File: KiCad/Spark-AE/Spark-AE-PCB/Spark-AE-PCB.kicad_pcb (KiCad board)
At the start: 2 copper layers, 50 x 100 mm, 21 parts, among them J1 SSM-120-L-SV-BE, J2 SSM-120-L-SV-BE, J3 Conn_02x10_Odd_Even, J4 Conn_02x05_Odd_Even, J5 Conn_01x08_Socket, J6 Conn_01x08_Socket, J7 UJ32-C-V-G-TH-5-P24-TR, SW1 SW_Push, SW2 SW_Push, U1 PJS008U-3000-0, U2 Daisy_Seed

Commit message: moving over progress from "Shock" (see desc)
I attempted to create this Daisy Pod clone as an AE-1U module called the "Shock". As expected I couldn't make it work.

I've moved my progress on the "Shock" schematic over to and replacing the work on the "Spark".

I plan to go back to make the "Shock" a stripped down version of the "Spark" in an AE-1U format.
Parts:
- removed ? (x5): , 
- removed J1, J2: SSM-120-L-SV-BE, clectric-diy:SAMTEC_SSM-120-L-SV-BE
- removed J3: Conn_02x10_Odd_Even, Connector_PinHeader_2.54mm:PinHeader_2x10_P2.54mm_Vertical
- removed J4: Conn_02x05_Odd_Even, Connector_PinHeader_2.54mm:PinHeader_2x05_P2.54mm_Vertical
- removed J5, J6: Conn_01x08_Socket, Connector_PinSocket_2.54mm:PinSocket_1x08_P2.54mm_Vertical
- removed J7: UJ32-C-V-G-TH-5-P24-TR, clectric-diy:SAMESKY_UJ32-C-V-G-TH-5-P24-TR
- removed LED1, LED2: WS2812B-V5/W, clectric-diy:LED-SMD_4P-L5.0-W5.0-TL-1
- removed R1, R2: RK09K1130A8G, clectric-diy:RES-TH_RK09K113004U
- removed S1: PEL12T-4225S-S1024, clectric-diy:PEL12T4225SS1024
- removed SW1, SW2: SW_Push, Button_Switch_THT:SW_PUSH_6mm
- removed U1: PJS008U-3000-0, clectric-diy:PJS008U-3000-0
- removed U2: Daisy_Seed, clectric-diy:DAISY_SEED
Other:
- board outline removed

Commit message: initial committ of completely reworked schematic. thanks gemini!
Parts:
- added ENC1: PEL12T-4225S-S1024, clectric-diy:PEL12T4225SS1024, F.Cu at (119.6, 129.2)
- added J1: Conn_01x20_Pin, clectric-diy:Connector_PinSocket-1x20-P2.54mm_Mill-Max_315-13-120-41-004000, B.Cu at (134.3, 122.5)
- added J2: Conn_01x20_Pin, clectric-diy:Connector_PinSocket-1x20-P2.54mm_Mill-Max_315-13-120-41-004000, B.Cu at (149.6, 74.2)
- added J3: Conn_01x09_Socket, Connector_PinSocket_2.54mm:PinSocket_1x09_P2.54mm_Vertical, F.Cu at (109.3, 49.8)
- added J4: Conn_01x09_Socket, Connector_PinSocket_2.54mm:PinSocket_1x09_P2.54mm_Vertical, F.Cu at (154.7, 49.8)
- added J5: Conn_02x05_Odd_Even, Connector_PinHeader_2.54mm:PinHeader_2x05_P2.54mm_Vertical, B.Cu at (154.7, 128.8)
- added LED1: A-SP1943B1GHR6C-C01-2T, clectric-diy:LED-SMD_4P-L1.6-W1.5-BL_A-SP1943B1GHR6C-C01-2T, F.Cu at (119.6, 97.7)
- added LED2: A-SP1943B1GHR6C-C01-2T, clectric-diy:LED-SMD_4P-L1.6-W1.5-BL_A-SP1943B1GHR6C-C01-2T, F.Cu at (119.6, 112.9)
- added POT1: RK09K1130D62, clectric-diy:RK09K1130D62, F.Cu at (119.6, 101.2)
- added POT2: RK09K1130D62, clectric-diy:RK09K1130D62, F.Cu at (119.6, 116.4)
- added SW1: SW_Push, Button_Switch_THT:SW_PUSH_6mm, F.Cu at (145.2, 79.1)
- added SW2: SW_Push, Button_Switch_THT:SW_PUSH_6mm, F.Cu at (145.2, 91.1)
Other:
- board outline added: 50 x 100 mm
- board text added: "&"

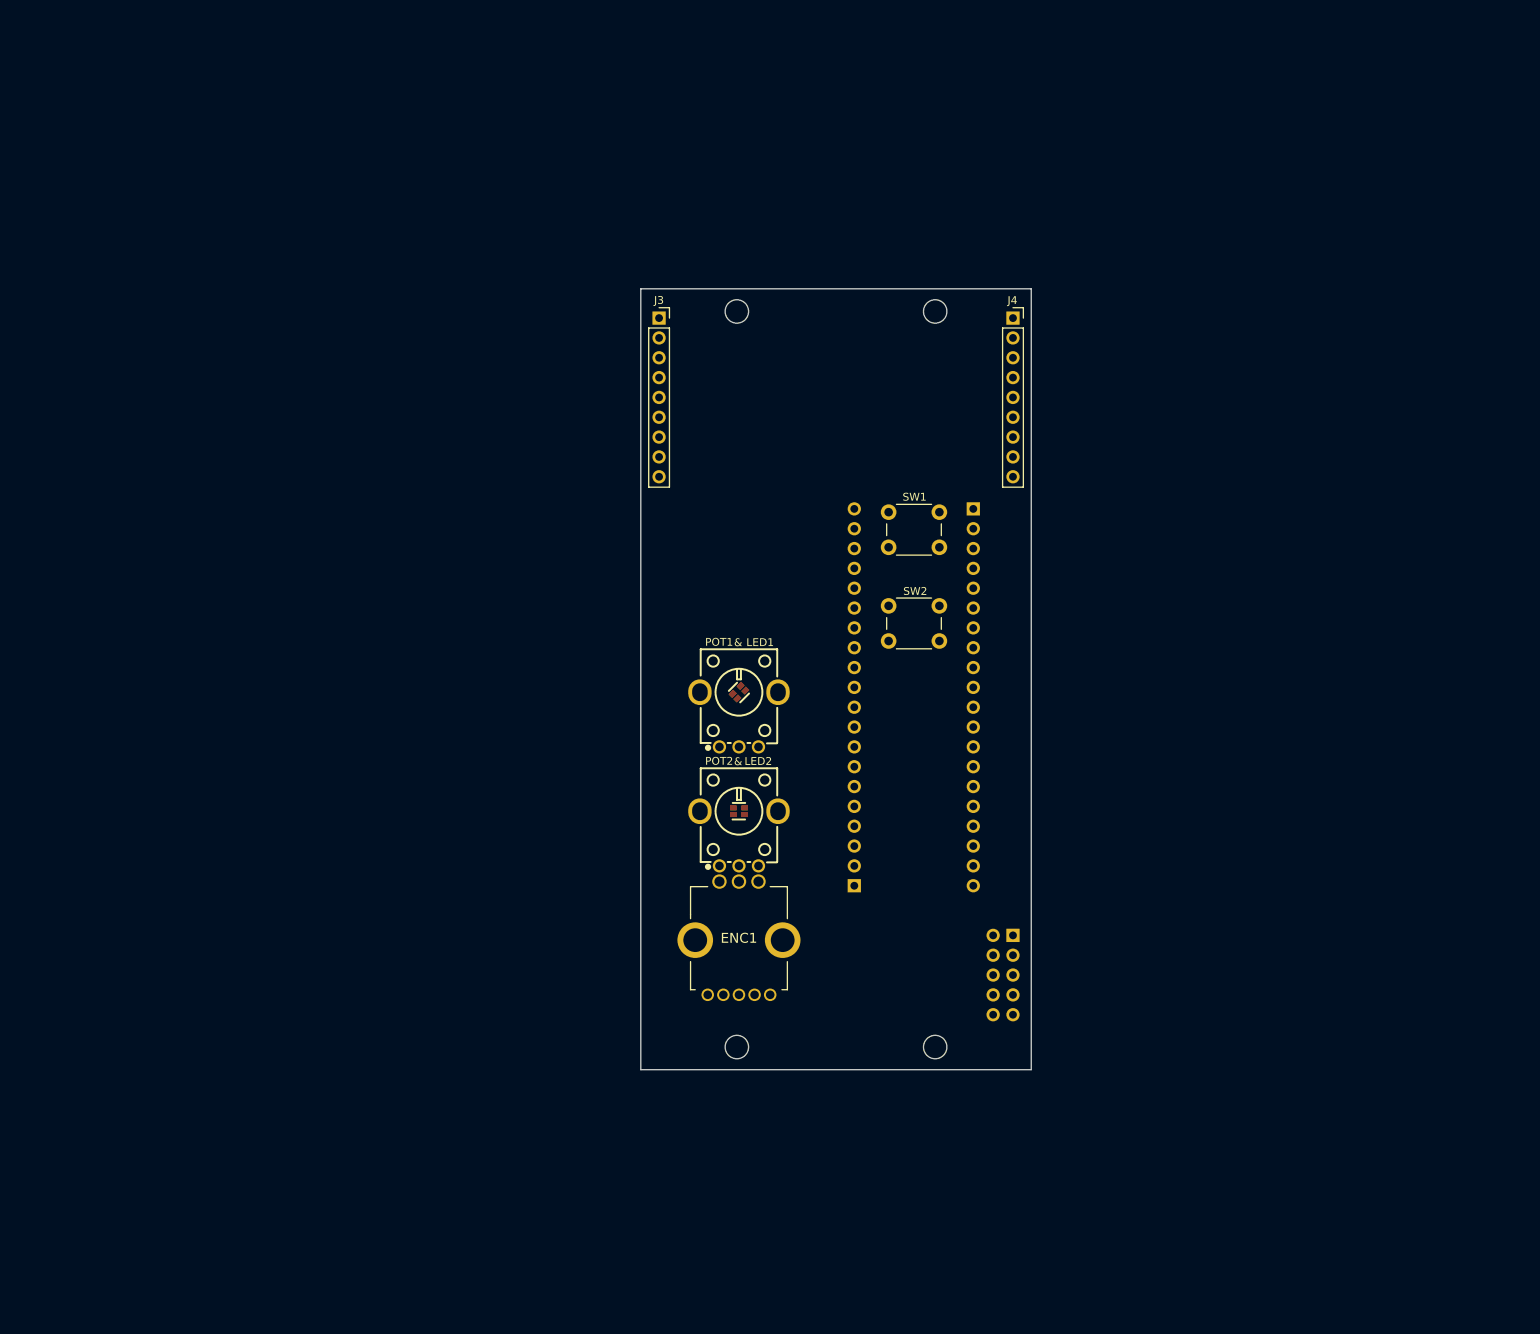
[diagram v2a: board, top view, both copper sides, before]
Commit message: assigned footprints & sorted ratsnest
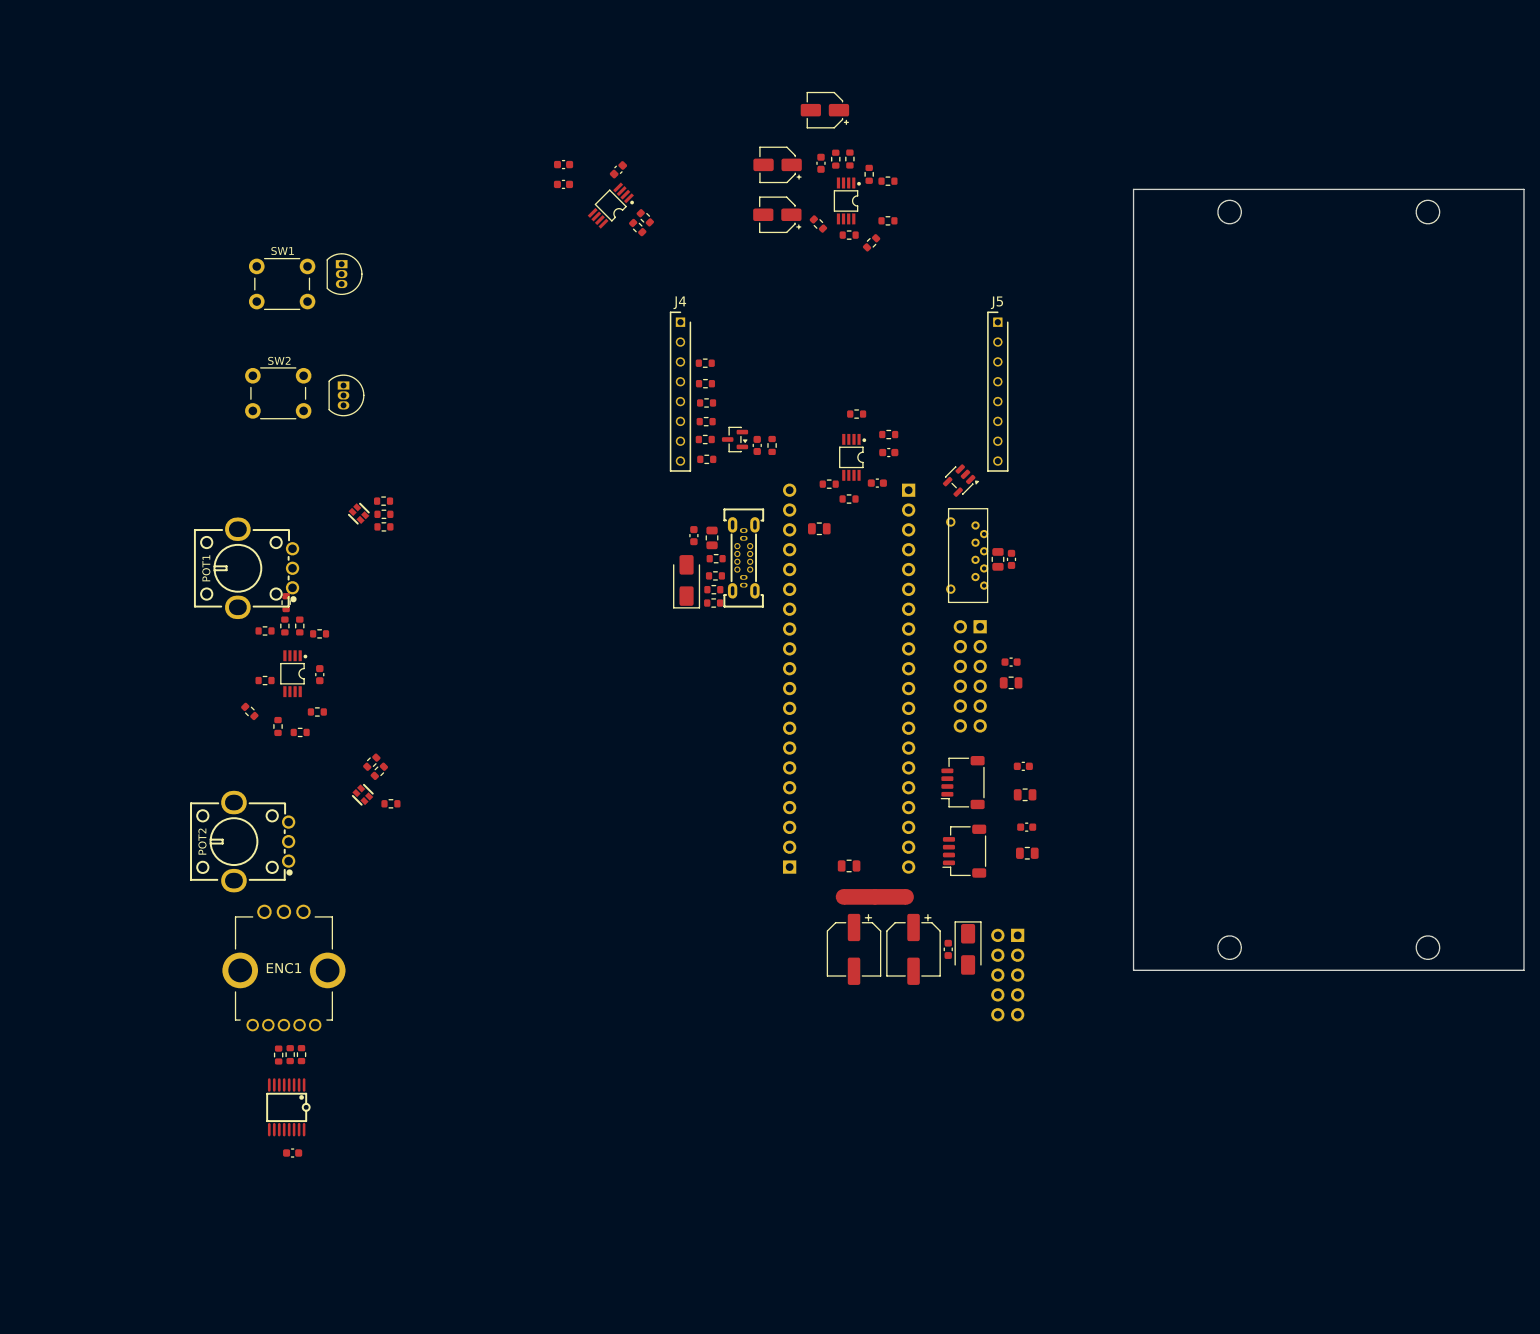
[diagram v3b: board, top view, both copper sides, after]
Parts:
- added C1: 220uF, Capacitor_SMD:CP_Elec_6.3x5.4, F.Cu at (134.3, 130.6)
- added C10: 10uF, Capacitor_SMD:CP_Elec_4x5.4, F.Cu at (124.5, 30.1)
- added C11: 10uF, Capacitor_SMD:CP_Elec_4x5.4, F.Cu at (124.5, 36.5)
- added C12: 100nF, Capacitor_SMD:C_0603_1608Metric, F.Cu at (130.1, 29.9)
- added C13: 10uF, Capacitor_SMD:CP_Elec_4x5.4, F.Cu at (130.6, 23.1)
- added C14: 10uF, Capacitor_SMD:C_0805_2012Metric, F.Cu at (152.7, 80.7)
- added C15: 100nF, Capacitor_SMD:C_0603_1608Metric, F.Cu at (154.5, 80.7)
- added C16: 10nF, Capacitor_SMD:C_0603_1608Metric, F.Cu at (121.9, 66.1)
- added C17: 100nF, Capacitor_SMD:C_0603_1608Metric, F.Cu at (137.3, 70.9)
- added C18: 100nF, Capacitor_SMD:C_0603_1608Metric, F.Cu at (138.7, 67.0)
- added C19: 100nF, Capacitor_SMD:C_0603_1608Metric, F.Cu at (113.8, 77.6)
- added C2: 220uF, Capacitor_SMD:CP_Elec_6.3x5.4, F.Cu at (141.9, 130.6)
- added C20: 10uF, Capacitor_SMD:C_0805_2012Metric, F.Cu at (116.1, 77.9)
- added C21: 100nF, Capacitor_SMD:C_0603_1608Metric, F.Cu at (156.0, 107.2)
- added C22: 10uF, Capacitor_SMD:C_0805_2012Metric, F.Cu at (156.2, 110.8)
- added C23: 100nF, Capacitor_SMD:C_0603_1608Metric, F.Cu at (156.4, 115.0)
- added C24: 10uF, Capacitor_SMD:C_0805_2012Metric, F.Cu at (156.5, 118.3)
- added C25: 100nF, Capacitor_SMD:C_0603_1608Metric, F.Cu at (154.4, 93.8)
- added C26: 10uF, Capacitor_SMD:C_0805_2012Metric, F.Cu at (154.4, 96.5)
- added C3: 10uF, Capacitor_SMD:C_0805_2012Metric, F.Cu at (129.8, 76.7)
- added C4: 10uF, Capacitor_SMD:C_0805_2012Metric, F.Cu at (133.7, 119.9)
- added C5: 100nF, Capacitor_SMD:C_0603_1608Metric, F.Cu at (65.9, 95.4)
- added C6: 100nF, Capacitor_SMD:C_0603_1608Metric, F.Cu at (62.4, 156.7)
- added C7: 1uF, Capacitor_SMD:C_0603_1608Metric, F.Cu at (97.1, 30.1)
- added C8: 1uF, Capacitor_SMD:C_0603_1608Metric, F.Cu at (97.1, 32.6)
- added C9: 100nF, Capacitor_SMD:C_0603_1608Metric, F.Cu at (104.1, 30.8)
- added D1: SS14, Diode_SMD:D_SMA, F.Cu at (148.9, 130.6)
- added D2: BAT54S, Package_TO_SOT_SMD:SOT-23, F.Cu at (119.1, 65.3)
- added D3: 2214, Diode_SMD:D_SMA, F.Cu at (112.8, 83.4)
- added FB1: BLM18AG601, Inductor_SMD:L_0603_1608Metric, F.Cu at (146.4, 130.6)
- added J6: I2C_IN, Connector_JST:JST_SH_SM04B-SRSS-TB_1x04-1MP_P1.00mm_Horizontal, F.Cu at (148.3, 109.2)
- added J7: I2C_OUT, Connector_JST:JST_SH_SM04B-SRSS-TB_1x04-1MP_P1.00mm_Horizontal, F.Cu at (148.5, 118.0)
- added J8: Conn_02x06_Top_Bottom, Connector_PinHeader_2.54mm:PinHeader_2x06_P2.54mm_Vertical, B.Cu at (150.4, 89.3)
- added NT1: NetTie_3_Tee, NetTie:NetTie-3_SMD_Pad2.0mm, F.Cu at (137.0, 123.9)
- added Q1: 2N3904, Package_TO_SOT_THT:TO-92_Inline, F.Cu at (68.7, 42.9)
- added Q2: 2N3904, Package_TO_SOT_THT:TO-92_Inline, F.Cu at (68.9, 58.4)
- added R1: 1K8, Resistor_SMD:R_0603_1608Metric, F.Cu at (115.4, 60.6)
- added R10: 100K, Resistor_SMD:R_0603_1608Metric, F.Cu at (65.9, 90.2)
- added R12: 10K, Resistor_SMD:R_0603_1608Metric, F.Cu at (115.3, 58.2)
- added R13: 1K8, Resistor_SMD:R_0603_1608Metric, F.Cu at (115.4, 63.0)
- added R14: 1K, Resistor_SMD:R_0603_1608Metric, F.Cu at (75.0, 112.0)
- added R15: 100R, Resistor_SMD:R_0603_1608Metric, F.Cu at (73.5, 107.8)
- added R16: 100R, Resistor_SMD:R_0603_1608Metric, F.Cu at (72.5, 106.6)
- added R17: 3K3, Resistor_SMD:R_0603_1608Metric, F.Cu at (58.9, 96.2)
- added R18: 100K, Resistor_SMD:R_0603_1608Metric, F.Cu at (56.9, 100.1)
- added R19: 100K, Resistor_SMD:R_0603_1608Metric, F.Cu at (60.5, 102.1)
- added R2: 3K3, Resistor_SMD:R_0603_1608Metric, F.Cu at (61.6, 86.2)
- added R20: 100K, Resistor_SMD:R_0603_1608Metric, F.Cu at (65.6, 100.2)
- added R21: 100K, Resistor_SMD:R_0603_1608Metric, F.Cu at (63.4, 102.8)
- added R23: 1K, Resistor_SMD:R_0603_1608Metric, F.Cu at (63.5, 144.1)
- added R24: 100R, Resistor_SMD:R_0603_1608Metric, F.Cu at (62.1, 144.1)
- added R25: 100R, Resistor_SMD:R_0603_1608Metric, F.Cu at (60.6, 144.1)
- added R26: 4K7, Resistor_SMD:R_0603_1608Metric, F.Cu at (106.6, 38.2)
- added R27: 4K7, Resistor_SMD:R_0603_1608Metric, F.Cu at (107.6, 36.9)
- added R28: 100K, Resistor_SMD:R_0603_1608Metric, F.Cu at (133.8, 29.4)
- added R29: 100K, Resistor_SMD:R_0603_1608Metric, F.Cu at (133.7, 39.1)
- added R3: 10K, Resistor_SMD:R_0603_1608Metric, F.Cu at (115.2, 55.5)
- added R30: 10K, Resistor_SMD:R_0603_1608Metric, F.Cu at (132.0, 29.4)
- added R31: 10K, Resistor_SMD:R_0603_1608Metric, F.Cu at (129.7, 37.7)
- added R32: 100K, Resistor_SMD:R_0603_1608Metric, F.Cu at (136.2, 31.4)
- added R33: 100K, Resistor_SMD:R_0603_1608Metric, F.Cu at (136.5, 40.1)
- added R34: 15K, Resistor_SMD:R_0603_1608Metric, F.Cu at (138.6, 32.2)
- added R35: 15K, Resistor_SMD:R_0603_1608Metric, F.Cu at (138.6, 37.3)
- added R36: 10K, Resistor_SMD:R_0603_1608Metric, F.Cu at (115.2, 65.3)
- added R37: 10K, Resistor_SMD:R_0603_1608Metric, F.Cu at (123.8, 66.1)
- added R38: 1K8, Resistor_SMD:R_0603_1608Metric, F.Cu at (134.6, 62.1)
- added R39: 3K3, Resistor_SMD:R_0603_1608Metric, F.Cu at (115.4, 67.9)
- added R4: 100K, Resistor_SMD:R_0603_1608Metric, F.Cu at (61.4, 89.2)
- added R40: 5K1, Resistor_SMD:R_0603_1608Metric, F.Cu at (138.7, 64.7)
- added R41: 1K, Resistor_SMD:R_0603_1608Metric, F.Cu at (133.7, 72.9)
- added R42: 1K, Resistor_SMD:R_0603_1608Metric, F.Cu at (131.1, 71.0)
- added R43: 10K, Resistor_SMD:R_0603_1608Metric, F.Cu at (116.5, 82.8)
- added R44: 10K, Resistor_SMD:R_0603_1608Metric, F.Cu at (116.6, 80.6)
- added R45: 5K1, Resistor_SMD:R_0603_1608Metric, F.Cu at (116.3, 86.3)
- added R46: 5K1, Resistor_SMD:R_0603_1608Metric, F.Cu at (116.3, 84.5)
- added R5: 100K, Resistor_SMD:R_0603_1608Metric, F.Cu at (63.3, 89.2)
- added R6: 1K, Resistor_SMD:R_0603_1608Metric, F.Cu at (74.1, 74.9)
- added R7: 100R, Resistor_SMD:R_0603_1608Metric, F.Cu at (74.1, 76.5)
- added R8: 100R, Resistor_SMD:R_0603_1608Metric, F.Cu at (74.1, 73.2)
- added R9: 100K, Resistor_SMD:R_0603_1608Metric, F.Cu at (58.9, 89.8)
- added U2: MCP6002-xMS, clectric-diy:Amplifier_Operational_Microchip_MCP6002T-I_MS, F.Cu at (62.4, 95.3)
- added U3: Driver_LED_PCA9633PW,118, clectric-diy:TSSOP-16_L5.0-W4.4-P0.64-LS6.4-BL, F.Cu at (61.6, 150.8)
- added U4: MCP6002-xMS, clectric-diy:Amplifier_Operational_Microchip_MCP6002T-I_MS, F.Cu at (103.2, 35.4)
- added U5: MCP6002-xMS, clectric-diy:Amplifier_Operational_Microchip_MCP6002T-I_MS, F.Cu at (133.3, 34.8)
- added U6: Connector_Micro_SD_Card_Yamaichi_PJS008U-3000-0, clectric-diy:PJS008U-3000-0, F.Cu at (148.4, 79.8)
- added U7: MCP6002-xMS, clectric-diy:Amplifier_Operational_Microchip_MCP6002T-I_MS, F.Cu at (134.0, 67.6)
- added U8: 74LVC1G125, Package_TO_SOT_SMD:SOT-23-5, F.Cu at (147.8, 70.6)
- added USB1: USB_C_Receptacle_G-Switch_GT-USB-7038A, clectric-diy:USB_C_Receptacle_G-Switch_GT-USB-7038A, F.Cu at (120.2, 80.5)
- ENC1: value PEL12T-4225S-S1024 -> RotaryEncoder_Switch_Bourns_PEL12T-4225S-S1024; footprint clectric-diy:PEL12T4225SS1024 -> clectric-diy:RotaryEncoder_Switch_Bourns_PEL12T-4225S-S1024
- J1, J2: value Conn_01x20_Pin -> Conn_01x20_Socket; footprint clectric-diy:Connector_PinSocket-1x20-P2.54mm_Mill-Max_315-13-120-41-004000 -> clectric-diy:Connector_PinSocket-1x20-P2.54mm-H1.27mm_Mill-Max_315-13-120-41-004000
- J3: value Conn_01x09_Socket -> AE_BUS; footprint Connector_PinSocket_2.54mm:PinSocket_1x09_P2.54mm_Vertical -> Connector_PinHeader_2.54mm:PinHeader_2x05_P2.54mm_Vertical; moved to B.Cu
- J4: value Conn_01x09_Socket -> Inputs; footprint Connector_PinSocket_2.54mm:PinSocket_1x09_P2.54mm_Vertical -> clectric-diy:Connector_PinSocket-1x08-P2.54mm-H8.5mm_Preci-Dip_801-87-008-10-005101
- J5: value Conn_02x05_Odd_Even -> Outputs; footprint Connector_PinHeader_2.54mm:PinHeader_2x05_P2.54mm_Vertical -> clectric-diy:Connector_PinSocket-1x08-P2.54mm-H8.5mm_Preci-Dip_801-87-008-10-005101; moved to F.Cu
- LED1, LED2: footprint clectric-diy:LED-SMD_4P-L1.6-W1.5-BL_A-SP1943B1GHR6C-C01-2T -> clectric-diy:LED_ARGB_Amicc_A-SP1943B1GHR6C-C01-2T
- POT1, POT2: footprint clectric-diy:RK09K1130D62 -> clectric-diy:Potentiometer_THT_Alps_RK09K1130D62
- moved J3 91.4 mm to (155.2, 128.8), turned to 180 degrees
- moved SW1 86.8 mm to (64.3, 47.6)
- moved SW2 86.6 mm to (63.8, 61.6)
- moved J5 78.5 mm to (152.7, 50.3), turned to 90 degrees
- moved POT1 63.7 mm to (58.9, 81.8), turned to 90 degrees
- moved POT2 61.2 mm to (58.4, 116.8), turned to 90 degrees
- moved ENC1 58.4 mm to (61.3, 133.1)
- moved LED1 53.8 mm to (70.9, 74.8), turned to 135 degrees
- moved LED2 48.2 mm to (71.4, 110.8), turned to 135 degrees
- moved J4 42.6 mm to (112.1, 50.3), turned to 90 degrees
- moved J1 8.62 mm to (126.0, 120.1)
- moved J2 8.62 mm to (141.3, 71.8)
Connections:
- ENC1 pad 3: Net-(ENC1-COM) -> ENC_CLICK
- ENC1 pad 5: +5V -> 3V3_D
- ENC1 pad A1: Net-(C1-Pad1) -> ENC_A
- ENC1 pad B1: Net-(C2-Pad1) -> ENC_B
- ENC1 pad C1: DGND -> GNDD
- ENC1 pad MH1: DGND -> GNDD
- ENC1 pad MH2: DGND -> GNDD
- J1 pad 1: +3V3_A -> 3V3_A
- J1 pad 10: LED_2_B -> LED2_B
- J1 pad 11: LED_2_G -> LED2_G
- J1 pad 14: TAC_SWITCH_1 -> SW1
- J1 pad 15: TAC_SWITCH_2 -> SW2
- J1 pad 16: USB_OTG_FS_D- -> USB_D-
- J1 pad 17: USB_OTG_FS_D+ -> USB_D+
- J1 pad 18: +3V3_D -> 3V3_D
- J1 pad 19: +5V -> 5V
- J1 pad 2: POT_2 -> POT2
- J1 pad 20: DGND -> GNDD
- J1 pad 4: LED_2_R -> LED2_R
- J1 pad 5: LED_1_B -> LED1_B
- J1 pad 6: LED_1_G -> LED1_G
- J1 pad 7: LED_1_R -> LED1_R
- J1 pad 8: POT_1 -> POT1
- J2 pad 1: USB_OTG_FS_ID -> D0
- J2 pad 20: AGND -> GNDA
- J2 pad 8: SPI_NSS -> SPI_CS
- J3 pad 1: unconnected-(J1-Pin_1-Pad1) -> 5V
- J3 pad 2: unconnected-(J1-Pin_2-Pad2) -> 5V
- J3 pad 3: unconnected-(J1-Pin_3-Pad3) -> GND
- J3 pad 4: unconnected-(J1-Pin_4-Pad4) -> GND
- J4 pad 1: unconnected-(J2-Pin_1-Pad1) -> AUDIO_AE_IN_1
- J4 pad 2: unconnected-(J2-Pin_2-Pad2) -> AUDIO_AE_IN_2
- J4 pad 3: unconnected-(J2-Pin_3-Pad3) -> SW1_CV
- J4 pad 4: unconnected-(J2-Pin_4-Pad4) -> SW2_CV
- J4 pad 5: unconnected-(J2-Pin_5-Pad5) -> POT1_CV
- J4 pad 6: unconnected-(J2-Pin_6-Pad6) -> POT2_CV
- J4 pad 7: unconnected-(J2-Pin_7-Pad7) -> A1_D16_AE_IN
- J4 pad 8: unconnected-(J2-Pin_8-Pad8) -> D14_AE_IN
- J5 pad 1: +5V -> AUDIO_AE_OUT_1
- J5 pad 2: +5V -> AUDIO_AE_OUT_1
- J5 pad 3: GND -> AUDIO_AE_OUT_2
- J5 pad 4: GND -> AUDIO_AE_OUT_2
- J5 pad 5: CV -> unconnected-(J5-Pin_5-Pad5)
- J5 pad 6: GATE -> unconnected-(J5-Pin_6-Pad6)
- J5 pad 7: START -> A7_D22_AE_OUT
- J5 pad 8: CLOCK -> D0_AE_OUT
- LED1 pad 3: +3V3_D -> 3V3_D
- LED2 pad 3: +3V3_D -> 3V3_D
- POT1 pad 1: AGND -> 3V3_A
- POT1 pad 2: POT_1 -> Net-(POT1-Pad2)
- POT1 pad 3: +3V3_A -> GNDA
- POT1 pad 4: AGND -> GNDA
- POT1 pad 5: AGND -> GNDA
- POT2 pad 1: AGND -> 3V3_A
- POT2 pad 2: POT_2 -> Net-(POT2-Pad2)
- POT2 pad 3: +3V3_A -> GNDA
- POT2 pad 4: AGND -> GNDA
- POT2 pad 5: AGND -> GNDA
- SW1 pad 1: TAC_SWITCH_1 -> SW_1
- SW1 pad 2: AGND -> GNDD
- SW2 pad 1: TAC_SWITCH_2 -> SW_2
- SW2 pad 2: AGND -> GNDD
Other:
- board text removed: "&"
